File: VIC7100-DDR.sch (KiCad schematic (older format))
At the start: 13 parts, among them U13 VIC7100

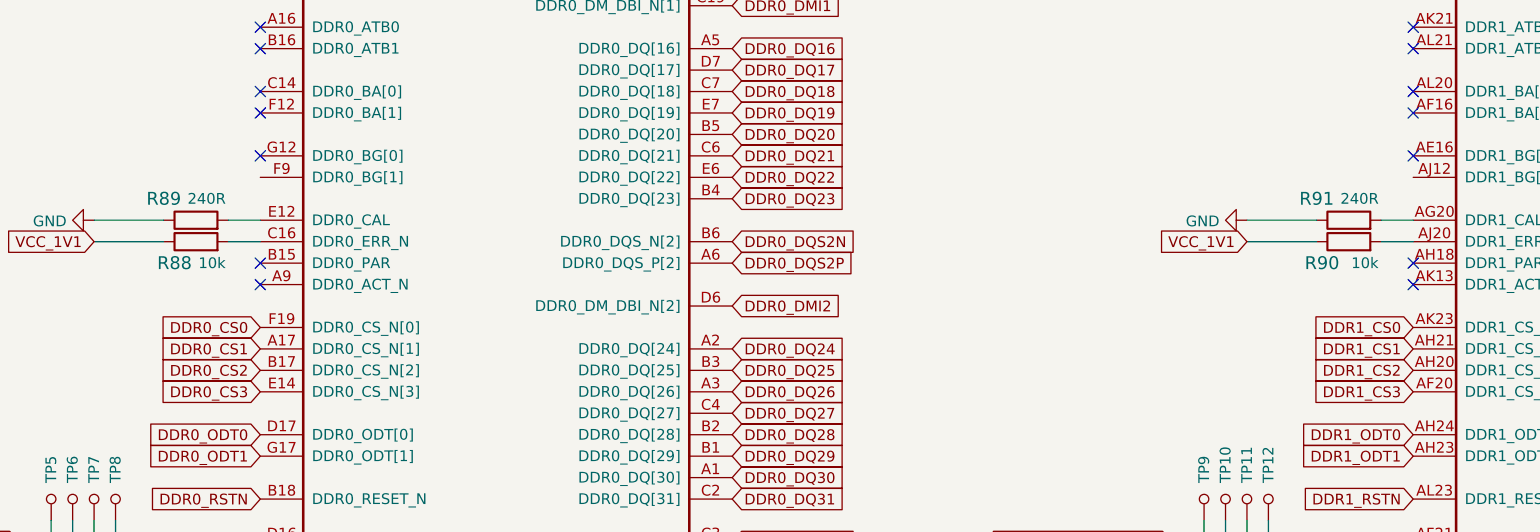
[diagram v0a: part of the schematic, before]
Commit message: Finished component placement
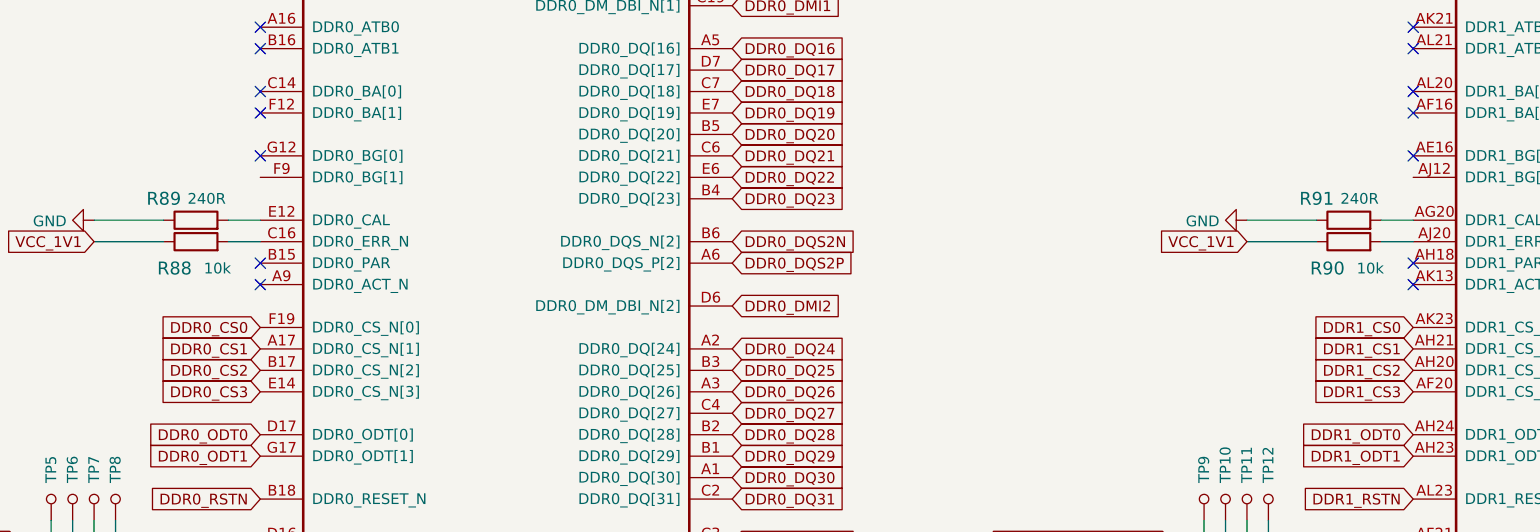
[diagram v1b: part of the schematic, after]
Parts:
- removed R88, R90: R_10k_0402, arvsom-footprints:0402-res, symbol arvsom:R_10k_0402
- added R88, R90: R_10k_0201, arvsom-footprints:0201-res, symbol arvsom:R_10k_0201
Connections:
- net VCC_1V1: now also R88.1, R90.1
- net at U13.C16 (DDR0_ERR_N): now also R88.2
- net at U13.AJ20 (DDR1_ERR_N): now also R90.2
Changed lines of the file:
@@
 Wire Wire Line
 	4200 5850 4050 5850
-$Comp
-L arvsom:R_10k_0402 R88
-U 1 1 615F0DBD
-P 3900 5950
-F 0 "R88" H 3800 5850 60  0000 C CNN
-F 1 "R_10k_0402" H 3900 5800 60  0001 C CNN
-F 2 "arvsom-footprints:0402-res" H 4100 6150 60  0001 L CNN
-F 3 "" H 3900 5950 50  0001 C CNN
-F 4 "VISHAY" H 4100 6350 60  0001 L CNN "Manufacturer"
-F 5 "CRCW040210K0FKEDHP" H 4100 6250 60  0001 L CNN "MPN"
-F 6 "10k" H 3975 5850 50  0000 C CNN "Val"
-	1    3900 5950
-	1    0    0    -1
-$EndComp
 Wire Wire Line
 	4050 5950 4200 5950
@@
 Wire Wire Line
 	9575 5850 9425 5850
-$Comp
-L arvsom:R_10k_0402 R90
-U 1 1 6170D5F7
-P 9275 5950
-F 0 "R90" H 9150 5850 60  0000 C CNN
-F 1 "R_10k_0402" H 9275 5800 60  0001 C CNN
-F 2 "arvsom-footprints:0402-res" H 9475 6150 60  0001 L CNN
-F 3 "" H 9275 5950 50  0001 C CNN
-F 4 "VISHAY" H 9475 6350 60  0001 L CNN "Manufacturer"
-F 5 "CRCW040210K0FKEDHP" H 9475 6250 60  0001 L CNN "MPN"
-F 6 "10k" H 9350 5850 50  0000 C CNN "Val"
-	1    9275 5950
-	1    0    0    -1
-$EndComp
 Wire Wire Line
 	9425 5950 9575 5950
@@
 Text GLabel 4200 4650 0    50   Input ~ 0
 DDR0_CK1_N
+$Comp
+L arvsom:R_10k_0201 R90
+U 1 1 61F83541
+P 9275 5950
+F 0 "R90" H 9175 5825 60  0000 C CNN
+F 1 "R_10k_0201" H 9275 5800 60  0001 C CNN
+F 2 "arvsom-footprints:0201-res" H 9475 6150 60  0001 L CNN
+F 3 "" H 9275 5950 50  0001 C CNN
+F 4 "YAGEO" H 9475 6350 60  0001 L CNN "Manufacturer"
+F 5 "RC0201FR-0710KL" H 9475 6250 60  0001 L CNN "MPN"
+F 6 "10k" H 9375 5825 50  0000 C CNN "Val"
+	1    9275 5950
+	1    0    0    -1
+$EndComp
+$Comp
+L arvsom:R_10k_0201 R88
+U 1 1 61FA9D7F
+P 3900 5950
+F 0 "R88" H 3800 5825 60  0000 C CNN
+F 1 "R_10k_0201" H 3900 5800 60  0001 C CNN
+F 2 "arvsom-footprints:0201-res" H 4100 6150 60  0001 L CNN
+F 3 "" H 3900 5950 50  0001 C CNN
+F 4 "YAGEO" H 4100 6350 60  0001 L CNN "Manufacturer"
+F 5 "RC0201FR-0710KL" H 4100 6250 60  0001 L CNN "MPN"
+F 6 "10k" H 4000 5825 50  0000 C CNN "Val"
+	1    3900 5950
+	1    0    0    -1
+$EndComp
 $EndSCHEMATC

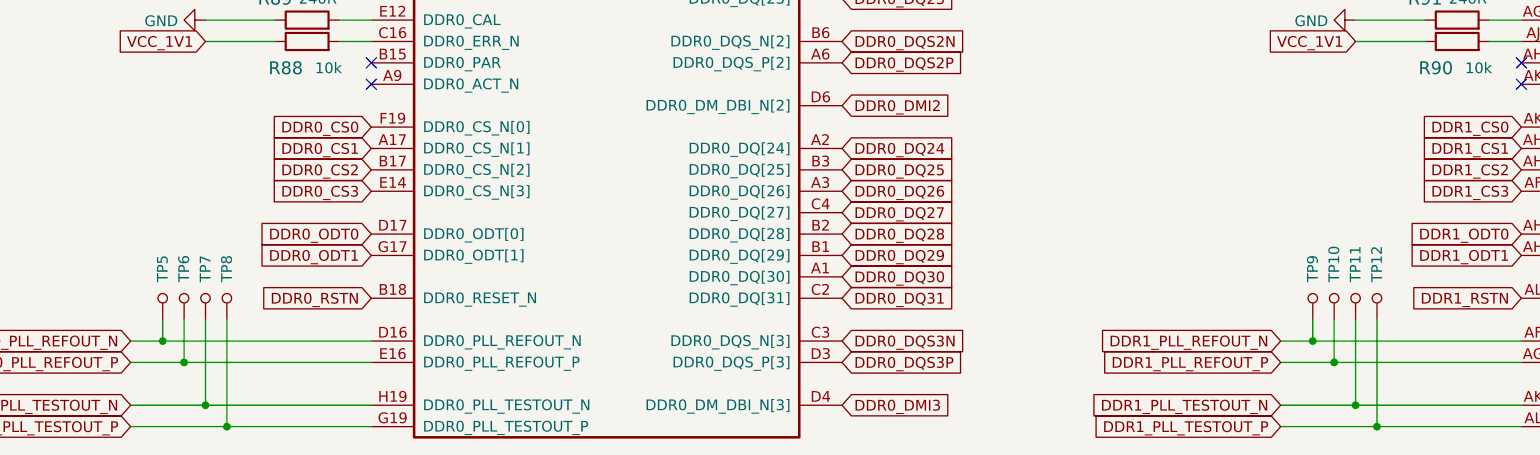
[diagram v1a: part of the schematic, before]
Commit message: Layout: 5v8 dcdc, clocks, SPIFlash, testpoints
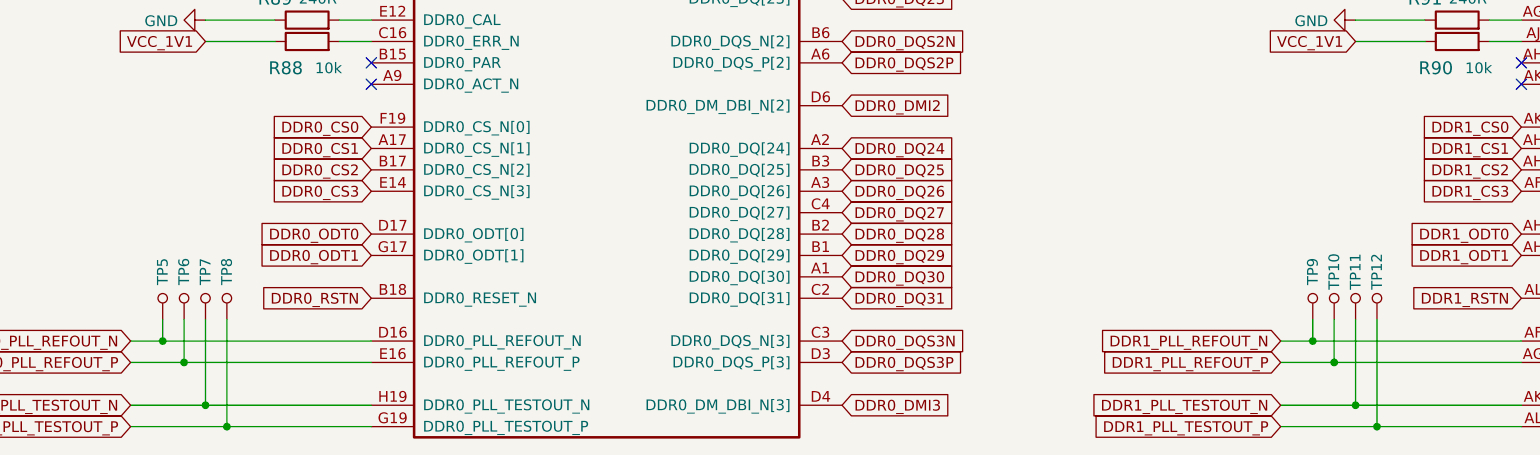
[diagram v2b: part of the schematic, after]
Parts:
- removed TP10, TP11, TP12, TP5, TP6, TP7, TP8, TP9: TP_SMD1MM, arvsom-footprints:Testpoint_smd_1mm, symbol arvsom:TP_SMD1MM
- added TP10, TP11, TP12, TP5, TP6, TP7, TP8, TP9: TP_SMD_0_75MM, arvsom-footprints:Testpoint_smd_0_75mm, symbol arvsom:TP_SMD_0_75MM
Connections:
- net DDR0_PLL_REFOUT_N: now also TP5.1
- net DDR0_PLL_REFOUT_P: now also TP6.1
- net DDR0_PLL_TESTOUT_N: now also TP7.1
- net DDR0_PLL_TESTOUT_P: now also TP8.1
- net DDR1_PLL_REFOUT_N: now also TP9.1
- net DDR1_PLL_REFOUT_P: now also TP10.1
- net DDR1_PLL_TESTOUT_N: now also TP11.1
- net DDR1_PLL_TESTOUT_P: now also TP12.1
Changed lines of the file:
@@
 Wire Wire Line
 	4200 7750 3525 7750
-$Comp
-L arvsom:TP_SMD1MM TP5
-U 1 1 61630E41
-P 3225 7150
-F 0 "TP5" V 3225 7075 50  0000 R CNN
-F 1 "TP_SMD1MM" H 3225 7050 50  0001 C CNN
-F 2 "arvsom-footprints:Testpoint_smd_1mm" H 3425 7350 60  0001 L CNN
-F 3 "" H 3425 7450 60  0001 L CNN
-	1    3225 7150
-	-1   0    0    1
-$EndComp
-$Comp
-L arvsom:TP_SMD1MM TP6
-U 1 1 61631802
-P 3325 7150
-F 0 "TP6" V 3325 7075 50  0000 R CNN
-F 1 "TP_SMD1MM" H 3325 7050 50  0001 C CNN
-F 2 "arvsom-footprints:Testpoint_smd_1mm" H 3525 7350 60  0001 L CNN
-F 3 "" H 3525 7450 60  0001 L CNN
-	1    3325 7150
-	-1   0    0    1
-$EndComp
-$Comp
-L arvsom:TP_SMD1MM TP7
-U 1 1 6163202C
-P 3425 7150
-F 0 "TP7" V 3425 7075 50  0000 R CNN
-F 1 "TP_SMD1MM" H 3425 7050 50  0001 C CNN
-F 2 "arvsom-footprints:Testpoint_smd_1mm" H 3625 7350 60  0001 L CNN
-F 3 "" H 3625 7450 60  0001 L CNN
-	1    3425 7150
-	-1   0    0    1
-$EndComp
-$Comp
-L arvsom:TP_SMD1MM TP8
-U 1 1 61632781
-P 3525 7150
-F 0 "TP8" V 3525 7075 50  0000 R CNN
-F 1 "TP_SMD1MM" H 3525 7050 50  0001 C CNN
-F 2 "arvsom-footprints:Testpoint_smd_1mm" H 3725 7350 60  0001 L CNN
-F 3 "" H 3725 7450 60  0001 L CNN
-	1    3525 7150
-	-1   0    0    1
-$EndComp
 Wire Wire Line
 	3225 7250 3225 7350
@@
 Wire Wire Line
 	9575 7750 8900 7750
-$Comp
-L arvsom:TP_SMD1MM TP9
-U 1 1 6170D617
-P 8600 7150
-F 0 "TP9" V 8600 7075 50  0000 R CNN
-F 1 "TP_SMD1MM" H 8600 7050 50  0001 C CNN
-F 2 "arvsom-footprints:Testpoint_smd_1mm" H 8800 7350 60  0001 L CNN
-F 3 "" H 8800 7450 60  0001 L CNN
-	1    8600 7150
-	-1   0    0    1
-$EndComp
-$Comp
-L arvsom:TP_SMD1MM TP10
-U 1 1 6170D61D
-P 8700 7150
-F 0 "TP10" V 8700 7075 50  0000 R CNN
-F 1 "TP_SMD1MM" H 8700 7050 50  0001 C CNN
-F 2 "arvsom-footprints:Testpoint_smd_1mm" H 8900 7350 60  0001 L CNN
-F 3 "" H 8900 7450 60  0001 L CNN
-	1    8700 7150
-	-1   0    0    1
-$EndComp
-$Comp
-L arvsom:TP_SMD1MM TP11
-U 1 1 6170D623
-P 8800 7150
-F 0 "TP11" V 8800 7075 50  0000 R CNN
-F 1 "TP_SMD1MM" H 8800 7050 50  0001 C CNN
-F 2 "arvsom-footprints:Testpoint_smd_1mm" H 9000 7350 60  0001 L CNN
-F 3 "" H 9000 7450 60  0001 L CNN
-	1    8800 7150
-	-1   0    0    1
-$EndComp
-$Comp
-L arvsom:TP_SMD1MM TP12
-U 1 1 6170D629
-P 8900 7150
-F 0 "TP12" V 8900 7075 50  0000 R CNN
-F 1 "TP_SMD1MM" H 8900 7050 50  0001 C CNN
-F 2 "arvsom-footprints:Testpoint_smd_1mm" H 9100 7350 60  0001 L CNN
-F 3 "" H 9100 7450 60  0001 L CNN
-	1    8900 7150
-	-1   0    0    1
-$EndComp
 Wire Wire Line
 	8600 7250 8600 7350
@@
 	1    0    0    -1
 $EndComp
+$Comp
+L arvsom:TP_SMD_0_75MM TP?
+U 1 1 60EABE60
+P 3425 7150
+AR Path="/60805CC6/60EABE60" Ref="TP?"  Part="1"
+AR Path="/613A40EE/60EABE60" Ref="TP7"  Part="1"
+F 0 "TP7" V 3425 7025 50  0000 C CNN
+F 1 "TP_SMD_0_75MM" H 3425 7050 50  0001 C CNN
+F 2 "arvsom-footprints:Testpoint_smd_0_75mm" H 3625 7350 60  0001 L CNN
+F 3 "" H 3625 7450 60  0001 L CNN
+	1    3425 7150
+	-1   0    0    1
+$EndComp
+$Comp
+L arvsom:TP_SMD_0_75MM TP?
+U 1 1 60EABE66
+P 3325 7150
+AR Path="/60805CC6/60EABE66" Ref="TP?"  Part="1"
+AR Path="/613A40EE/60EABE66" Ref="TP6"  Part="1"
+F 0 "TP6" V 3325 7025 50  0000 C CNN
+F 1 "TP_SMD_0_75MM" H 3325 7050 50  0001 C CNN
+F 2 "arvsom-footprints:Testpoint_smd_0_75mm" H 3525 7350 60  0001 L CNN
+F 3 "" H 3525 7450 60  0001 L CNN
+	1    3325 7150
+	-1   0    0    1
+$EndComp
+$Comp
+L arvsom:TP_SMD_0_75MM TP?
+U 1 1 60EABE6C
+P 3225 7150
+AR Path="/60805CC6/60EABE6C" Ref="TP?"  Part="1"
+AR Path="/613A40EE/60EABE6C" Ref="TP5"  Part="1"
+F 0 "TP5" V 3225 7025 50  0000 C CNN
+F 1 "TP_SMD_0_75MM" H 3225 7050 50  0001 C CNN
+F 2 "arvsom-footprints:Testpoint_smd_0_75mm" H 3425 7350 60  0001 L CNN
+F 3 "" H 3425 7450 60  0001 L CNN
+	1    3225 7150
+	-1   0    0    1
+$EndComp
+$Comp
+L arvsom:TP_SMD_0_75MM TP?
+U 1 1 60EAC68C
+P 3525 7150
+AR Path="/60805CC6/60EAC68C" Ref="TP?"  Part="1"
+AR Path="/613A40EE/60EAC68C" Ref="TP8"  Part="1"
+F 0 "TP8" V 3525 7025 50  0000 C CNN
+F 1 "TP_SMD_0_75MM" H 3525 7050 50  0001 C CNN
+F 2 "arvsom-footprints:Testpoint_smd_0_75mm" H 3725 7350 60  0001 L CNN
+F 3 "" H 3725 7450 60  0001 L CNN
+	1    3525 7150
+	-1   0    0    1
+$EndComp
+$Comp
+L arvsom:TP_SMD_0_75MM TP?
+U 1 1 60EAF732
+P 8800 7150
+AR Path="/60805CC6/60EAF732" Ref="TP?"  Part="1"
+AR Path="/613A40EE/60EAF732" Ref="TP11"  Part="1"
+F 0 "TP11" V 8800 7025 50  0000 C CNN
+F 1 "TP_SMD_0_75MM" H 8800 7050 50  0001 C CNN
+F 2 "arvsom-footprints:Testpoint_smd_0_75mm" H 9000 7350 60  0001 L CNN
+F 3 "" H 9000 7450 60  0001 L CNN
+	1    8800 7150
+	-1   0    0    1
+$EndComp
+$Comp
+L arvsom:TP_SMD_0_75MM TP?
+U 1 1 60EAF738
+P 8700 7150
+AR Path="/60805CC6/60EAF738" Ref="TP?"  Part="1"
+AR Path="/613A40EE/60EAF738" Ref="TP10"  Part="1"
+F 0 "TP10" V 8700 7025 50  0000 C CNN
+F 1 "TP_SMD_0_75MM" H 8700 7050 50  0001 C CNN
+F 2 "arvsom-footprints:Testpoint_smd_0_75mm" H 8900 7350 60  0001 L CNN
+F 3 "" H 8900 7450 60  0001 L CNN
+	1    8700 7150
+	-1   0    0    1
+$EndComp
+$Comp
+L arvsom:TP_SMD_0_75MM TP?
+U 1 1 60EAF73E
+P 8600 7150
+AR Path="/60805CC6/60EAF73E" Ref="TP?"  Part="1"
+AR Path="/613A40EE/60EAF73E" Ref="TP9"  Part="1"
+F 0 "TP9" V 8600 7025 50  0000 C CNN
+F 1 "TP_SMD_0_75MM" H 8600 7050 50  0001 C CNN
+F 2 "arvsom-footprints:Testpoint_smd_0_75mm" H 8800 7350 60  0001 L CNN
+F 3 "" H 8800 7450 60  0001 L CNN
+	1    8600 7150
+	-1   0    0    1
+$EndComp
+$Comp
+L arvsom:TP_SMD_0_75MM TP?
+U 1 1 60EAF744
+P 8900 7150
+AR Path="/60805CC6/60EAF744" Ref="TP?"  Part="1"
+AR Path="/613A40EE/60EAF744" Ref="TP12"  Part="1"
+F 0 "TP12" V 8900 7025 50  0000 C CNN
+F 1 "TP_SMD_0_75MM" H 8900 7050 50  0001 C CNN
+F 2 "arvsom-footprints:Testpoint_smd_0_75mm" H 9100 7350 60  0001 L CNN
+F 3 "" H 9100 7450 60  0001 L CNN
+	1    8900 7150
+	-1   0    0    1
+$EndComp
 $EndSCHEMATC
